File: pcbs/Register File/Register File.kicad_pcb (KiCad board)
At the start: 4 copper layers, 160 parts, among them U201 74HCT574, U202 74HC245, U203 74HC245, U204 74HC245, U301 74HCT574, U302 74HC245, U303 74HC245, U304 74HC245, U401 74HCT574, U402 74HC245, U403 74HC245, U404 74HC245, U501 74HCT574, U502 74HC245, U503 74HC245, U504 74HC245, U601 74HCT574, U602 74HC245, U603 74HC245, U604 74HC245, U701 74HCT574, U702 74HC245, U703 74HC245, U704 74HC245, U801 74HCT574, U802 74HC245, U803 74HC245, U804 74HC245, U901 74HCT574, U902 74HC245, U903 74HC245, U904 74HC245

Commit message: More sketching
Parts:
- added D209: Blue, LED_SMD:LED_0603_1608Metric, F.Cu at (75.2, 52.1)
- added D210: Blue, LED_SMD:LED_0603_1608Metric, F.Cu at (74.9, 69.8)
- added D211: Blue, LED_SMD:LED_0603_1608Metric, F.Cu at (75.2, 87.6)
- added D309: Blue, LED_SMD:LED_0603_1608Metric, F.Cu at (105.7, 79.6)
- added D310: Blue, LED_SMD:LED_0603_1608Metric, F.Cu at (105.7, 82.2)
- added D311: Blue, LED_SMD:LED_0603_1608Metric, F.Cu at (105.7, 84.8)
- added D409: Blue, LED_SMD:LED_0603_1608Metric, F.Cu at (150.0, 149.0)
- added D410: Blue, LED_SMD:LED_0603_1608Metric, F.Cu at (150.0, 151.6)
- added D411: Blue, LED_SMD:LED_0603_1608Metric, F.Cu at (150.0, 154.1)
- added D509: Blue, LED_SMD:LED_0603_1608Metric, F.Cu at (170.1, 158.7)
- added D510: Blue, LED_SMD:LED_0603_1608Metric, F.Cu at (170.1, 161.3)
- added D511: Blue, LED_SMD:LED_0603_1608Metric, F.Cu at (170.1, 163.9)
- added D609: Blue, LED_SMD:LED_0603_1608Metric, F.Cu at (160.0, 168.5)
- added D610: Blue, LED_SMD:LED_0603_1608Metric, F.Cu at (160.0, 171.1)
- added D611: Blue, LED_SMD:LED_0603_1608Metric, F.Cu at (160.0, 173.7)
- added D709: Blue, LED_SMD:LED_0603_1608Metric, F.Cu at (170.1, 149.0)
- added D710: Blue, LED_SMD:LED_0603_1608Metric, F.Cu at (170.1, 151.6)
- added D711: Blue, LED_SMD:LED_0603_1608Metric, F.Cu at (170.1, 154.1)
- added D809: Blue, LED_SMD:LED_0603_1608Metric, F.Cu at (160.0, 158.7)
- added D810: Blue, LED_SMD:LED_0603_1608Metric, F.Cu at (160.0, 161.3)
- added D811: Blue, LED_SMD:LED_0603_1608Metric, F.Cu at (160.0, 163.9)
- added D909: Blue, LED_SMD:LED_0603_1608Metric, F.Cu at (150.0, 158.7)
- added D910: Blue, LED_SMD:LED_0603_1608Metric, F.Cu at (150.0, 161.3)
- added D911: Blue, LED_SMD:LED_0603_1608Metric, F.Cu at (150.0, 163.9)
- added R209: 4k7, Resistor_SMD:R_0603_1608Metric, F.Cu at (71.6, 52.1)
- added R210: 4k7, Resistor_SMD:R_0603_1608Metric, F.Cu at (71.4, 69.8)
- added R211: 4k7, Resistor_SMD:R_0603_1608Metric, F.Cu at (71.4, 87.6)
- added R309: 4k7, Resistor_SMD:R_0603_1608Metric, F.Cu at (109.7, 79.6)
- added R310: 4k7, Resistor_SMD:R_0603_1608Metric, F.Cu at (109.7, 82.1)
- added R311: 4k7, Resistor_SMD:R_0603_1608Metric, F.Cu at (109.7, 84.6)
- added R409: 4k7, Resistor_SMD:R_0603_1608Metric, F.Cu at (154.0, 148.9)
- added R410: 4k7, Resistor_SMD:R_0603_1608Metric, F.Cu at (154.0, 151.4)
- added R411: 4k7, Resistor_SMD:R_0603_1608Metric, F.Cu at (154.0, 153.9)
- added R509: 4k7, Resistor_SMD:R_0603_1608Metric, F.Cu at (174.1, 158.7)
- added R510: 4k7, Resistor_SMD:R_0603_1608Metric, F.Cu at (174.1, 161.2)
- added R511: 4k7, Resistor_SMD:R_0603_1608Metric, F.Cu at (174.1, 163.7)
- added R609: 4k7, Resistor_SMD:R_0603_1608Metric, F.Cu at (164.0, 168.5)
- added R610: 4k7, Resistor_SMD:R_0603_1608Metric, F.Cu at (164.0, 171.0)
- added R611: 4k7, Resistor_SMD:R_0603_1608Metric, F.Cu at (164.0, 173.5)
- added R709: 4k7, Resistor_SMD:R_0603_1608Metric, F.Cu at (174.1, 148.9)
- added R710: 4k7, Resistor_SMD:R_0603_1608Metric, F.Cu at (174.1, 151.4)
- added R711: 4k7, Resistor_SMD:R_0603_1608Metric, F.Cu at (174.1, 153.9)
- added R809: 4k7, Resistor_SMD:R_0603_1608Metric, F.Cu at (164.0, 158.7)
- added R810: 4k7, Resistor_SMD:R_0603_1608Metric, F.Cu at (164.0, 161.2)
- added R811: 4k7, Resistor_SMD:R_0603_1608Metric, F.Cu at (164.0, 163.7)
- added R909: 4k7, Resistor_SMD:R_0603_1608Metric, F.Cu at (154.0, 158.7)
- added R910: 4k7, Resistor_SMD:R_0603_1608Metric, F.Cu at (154.0, 161.2)
- added R911: 4k7, Resistor_SMD:R_0603_1608Metric, F.Cu at (154.0, 163.7)
- moved U302 3.59 mm to (96.5, 61.0)
- moved U203 2.54 mm to (71.1, 78.7)
- moved U204 2.54 mm to (71.1, 96.5)
- moved U202 2.54 mm to (71.1, 61.0)
- moved D301 2.54 mm to (91.4, 27.9)
- moved D302 2.54 mm to (91.4, 30.5)
- moved D303 2.54 mm to (91.4, 33.0)
- moved D304 2.54 mm to (91.4, 35.6)
- moved D305 2.54 mm to (91.4, 38.1)
- moved D306 2.54 mm to (91.4, 40.6)
- moved D307 2.54 mm to (91.4, 43.2)
- moved D308 2.54 mm to (91.4, 45.7)
- moved R301 2.54 mm to (96.5, 27.9)
- moved R302 2.54 mm to (96.5, 30.5)
- moved R303 2.54 mm to (96.5, 33.0)
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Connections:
- U202 pad 19: unconnected-(U202-CE-Pad19) -> /Register 0/~{A_{Enable}}
- U203 pad 19: unconnected-(U203-CE-Pad19) -> /Register 0/~{B_{Enable}}
- U204 pad 19: unconnected-(U204-CE-Pad19) -> /Register 0/~{C_{Enable}}
- U302 pad 19: unconnected-(U302-CE-Pad19) -> /Register 1/~{A_{Enable}}
- U303 pad 19: unconnected-(U303-CE-Pad19) -> /Register 1/~{B_{Enable}}
- U304 pad 19: unconnected-(U304-CE-Pad19) -> /Register 1/~{C_{Enable}}
- U402 pad 19: unconnected-(U402-CE-Pad19) -> /Register 2/~{A_{Enable}}
- U403 pad 19: unconnected-(U403-CE-Pad19) -> /Register 2/~{B_{Enable}}
- U404 pad 19: unconnected-(U404-CE-Pad19) -> /Register 2/~{C_{Enable}}
- U502 pad 19: unconnected-(U502-CE-Pad19) -> /Register 3/~{A_{Enable}}
- U503 pad 19: unconnected-(U503-CE-Pad19) -> /Register 3/~{B_{Enable}}
- U504 pad 19: unconnected-(U504-CE-Pad19) -> /Register 3/~{C_{Enable}}
- U602 pad 19: unconnected-(U602-CE-Pad19) -> /Register 4/~{A_{Enable}}
- U603 pad 19: unconnected-(U603-CE-Pad19) -> /Register 4/~{B_{Enable}}
- U604 pad 19: unconnected-(U604-CE-Pad19) -> /Register 4/~{C_{Enable}}
- U702 pad 19: unconnected-(U702-CE-Pad19) -> /Register 7/~{A_{Enable}}
- U703 pad 19: unconnected-(U703-CE-Pad19) -> /Register 7/~{B_{Enable}}
- U704 pad 19: unconnected-(U704-CE-Pad19) -> /Register 7/~{C_{Enable}}
- U802 pad 19: unconnected-(U802-CE-Pad19) -> /Register 6/~{A_{Enable}}
- U803 pad 19: unconnected-(U803-CE-Pad19) -> /Register 6/~{B_{Enable}}
- U804 pad 19: unconnected-(U804-CE-Pad19) -> /Register 6/~{C_{Enable}}
- U902 pad 19: unconnected-(U902-CE-Pad19) -> /Register 5/~{A_{Enable}}
- U903 pad 19: unconnected-(U903-CE-Pad19) -> /Register 5/~{B_{Enable}}
- U904 pad 19: unconnected-(U904-CE-Pad19) -> /Register 5/~{C_{Enable}}
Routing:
- net /Register 0/r0: track 0.00 -> 83.9 mm, vias 0 -> 1
- net /Register 0/r1: track 0.00 -> 81.1 mm, vias 0 -> 1
- net /Register 0/r2: track 0.00 -> 78.3 mm, vias 0 -> 1
- net /Register 0/r3: track 0.00 -> 73.8 mm, vias 0 -> 1
- net /Register 0/r5: track 0.00 -> 67.6 mm, vias 0 -> 1
- net /Register 0/r6: track 0.00 -> 67.1 mm, vias 0 -> 1
- net /Register 0/r4: track 0.00 -> 67.1 mm, vias 0 -> 1
- net /Register 0/r7: track 0.00 -> 64.6 mm, vias 0 -> 1
- net /Register 1/r0: track 0.00 -> 53.4 mm
- net /Register 1/r4: track 0.00 -> 38.2 mm
- net /Register 1/r3: track 0.00 -> 38.0 mm
- net /Register 1/r5: track 0.00 -> 15.9 mm
- net /Register 1/r6: track 0.00 -> 13.3 mm
- net /Register 1/r1: track 0.00 -> 12.8 mm
- net /Register 1/r7: track 0.00 -> 10.0 mm
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
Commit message: More connecting
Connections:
- D202 pad 2: unconnected-(D202-A-Pad2) -> /Register 0/r1
- D203 pad 2: unconnected-(D203-A-Pad2) -> /Register 0/r2
- D204 pad 2: unconnected-(D204-A-Pad2) -> /Register 0/r3
- D205 pad 2: unconnected-(D205-A-Pad2) -> /Register 0/r4
- D206 pad 2: unconnected-(D206-A-Pad2) -> /Register 0/r5
- D207 pad 2: unconnected-(D207-A-Pad2) -> /Register 0/r6
- D302 pad 2: unconnected-(D302-A-Pad2) -> /Register 1/r1
- D303 pad 2: unconnected-(D303-A-Pad2) -> /Register 1/r2
- D304 pad 2: unconnected-(D304-A-Pad2) -> /Register 1/r3
- D305 pad 2: unconnected-(D305-A-Pad2) -> /Register 1/r4
- D306 pad 2: unconnected-(D306-A-Pad2) -> /Register 1/r5
- D307 pad 2: unconnected-(D307-A-Pad2) -> /Register 1/r6
- D402 pad 2: unconnected-(D402-A-Pad2) -> /Register 2/r1
- D403 pad 2: unconnected-(D403-A-Pad2) -> /Register 2/r2
- D404 pad 2: unconnected-(D404-A-Pad2) -> /Register 2/r3
- D405 pad 2: unconnected-(D405-A-Pad2) -> /Register 2/r4
- D406 pad 2: unconnected-(D406-A-Pad2) -> /Register 2/r5
- D407 pad 2: unconnected-(D407-A-Pad2) -> /Register 2/r6
- D502 pad 2: unconnected-(D502-A-Pad2) -> /Register 3/r1
- D503 pad 2: unconnected-(D503-A-Pad2) -> /Register 3/r2
- D504 pad 2: unconnected-(D504-A-Pad2) -> /Register 3/r3
- D505 pad 2: unconnected-(D505-A-Pad2) -> /Register 3/r4
- D506 pad 2: unconnected-(D506-A-Pad2) -> /Register 3/r5
- D507 pad 2: unconnected-(D507-A-Pad2) -> /Register 3/r6
- D602 pad 2: unconnected-(D602-A-Pad2) -> /Register 4/r1
- D603 pad 2: unconnected-(D603-A-Pad2) -> /Register 4/r2
- D604 pad 2: unconnected-(D604-A-Pad2) -> /Register 4/r3
- D605 pad 2: unconnected-(D605-A-Pad2) -> /Register 4/r4
- D606 pad 2: unconnected-(D606-A-Pad2) -> /Register 4/r5
- D607 pad 2: unconnected-(D607-A-Pad2) -> /Register 4/r6
- D702 pad 2: unconnected-(D702-A-Pad2) -> /Register 7/r1
- D703 pad 2: unconnected-(D703-A-Pad2) -> /Register 7/r2
- D704 pad 2: unconnected-(D704-A-Pad2) -> /Register 7/r3
- D705 pad 2: unconnected-(D705-A-Pad2) -> /Register 7/r4
- D706 pad 2: unconnected-(D706-A-Pad2) -> /Register 7/r5
- D707 pad 2: unconnected-(D707-A-Pad2) -> /Register 7/r6
- D802 pad 2: unconnected-(D802-A-Pad2) -> /Register 6/r1
- D803 pad 2: unconnected-(D803-A-Pad2) -> /Register 6/r2
- D804 pad 2: unconnected-(D804-A-Pad2) -> /Register 6/r3
- D805 pad 2: unconnected-(D805-A-Pad2) -> /Register 6/r4
- D806 pad 2: unconnected-(D806-A-Pad2) -> /Register 6/r5
- D807 pad 2: unconnected-(D807-A-Pad2) -> /Register 6/r6
- D902 pad 2: unconnected-(D902-A-Pad2) -> /Register 5/r1
- D903 pad 2: unconnected-(D903-A-Pad2) -> /Register 5/r2
- D904 pad 2: unconnected-(D904-A-Pad2) -> /Register 5/r3
- D905 pad 2: unconnected-(D905-A-Pad2) -> /Register 5/r4
- D906 pad 2: unconnected-(D906-A-Pad2) -> /Register 5/r5
- D907 pad 2: unconnected-(D907-A-Pad2) -> /Register 5/r6
- U201 pad 1: unconnected-(U201-OE-Pad1) -> GND
- U201 pad 11: unconnected-(U201-Cp-Pad11) -> /Register 0/C_{write}
- U301 pad 1: unconnected-(U301-OE-Pad1) -> GND
- U301 pad 11: unconnected-(U301-Cp-Pad11) -> /Register 1/C_{write}
- U401 pad 1: unconnected-(U401-OE-Pad1) -> GND
- U401 pad 11: unconnected-(U401-Cp-Pad11) -> /Register 2/C_{write}
- U501 pad 1: unconnected-(U501-OE-Pad1) -> GND
- U501 pad 11: unconnected-(U501-Cp-Pad11) -> /Register 3/C_{write}
- U601 pad 1: unconnected-(U601-OE-Pad1) -> GND
- U601 pad 11: unconnected-(U601-Cp-Pad11) -> /Register 4/C_{write}
- U701 pad 1: unconnected-(U701-OE-Pad1) -> GND
- U701 pad 11: unconnected-(U701-Cp-Pad11) -> /Register 7/C_{write}
- U801 pad 1: unconnected-(U801-OE-Pad1) -> GND
- U801 pad 11: unconnected-(U801-Cp-Pad11) -> /Register 6/C_{write}
- U901 pad 1: unconnected-(U901-OE-Pad1) -> GND
- U901 pad 11: unconnected-(U901-Cp-Pad11) -> /Register 5/C_{write}

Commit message: Routing
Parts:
- moved R309 30.5 mm to (96.5, 52.1), turned to 180 degrees
- moved D309 28.0 mm to (100.6, 52.1), turned to 180 degrees
- moved R310 17.9 mm to (96.5, 69.8), turned to 180 degrees
- moved R311 13.5 mm to (96.5, 87.6), turned to 180 degrees
- moved D310 13.3 mm to (100.6, 69.8), turned to 180 degrees
- moved D311 5.82 mm to (100.6, 87.6), turned to 180 degrees
- moved U303 3.59 mm to (96.5, 78.7)
- moved U304 3.59 mm to (96.5, 96.5)
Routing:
- net /Register 1/r1: track 12.8 -> 103.2 mm, vias 0 -> 3
- net /Register 1/r2: track 9.50 -> 98.8 mm, vias 0 -> 3
- net /Register 1/r7: track 10.0 -> 74.2 mm, vias 0 -> 3
- net /Register 1/r6: track 13.3 -> 73.9 mm, vias 0 -> 3
- net /Register 1/r5: track 15.9 -> 73.7 mm, vias 0 -> 3
- net /Register 1/r3: track 38.0 -> 94.5 mm, vias 0 -> 3
- net /Register 1/r0: track 53.4 -> 107.5 mm, vias 0 -> 3
- net /Register 1/r4: track 38.2 -> 73.4 mm, vias 0 -> 3
- net /Register 0/C6: track 26.5 -> 57.1 mm, vias 0 -> 2
- net /Register 0/B5: track 0.00 -> 30.7 mm, vias 0 -> 2
- net /Register 0/C7: track 26.5 -> 57.1 mm, vias 0 -> 2
- net /Register 0/B7: track 0.00 -> 30.7 mm, vias 0 -> 2
- net /Register 0/B6: track 0.00 -> 30.7 mm, vias 0 -> 2
- net /Register 0/C5: track 26.5 -> 57.1 mm, vias 0 -> 2
- net /Register 0/B4: track 0.00 -> 30.7 mm, vias 0 -> 2
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
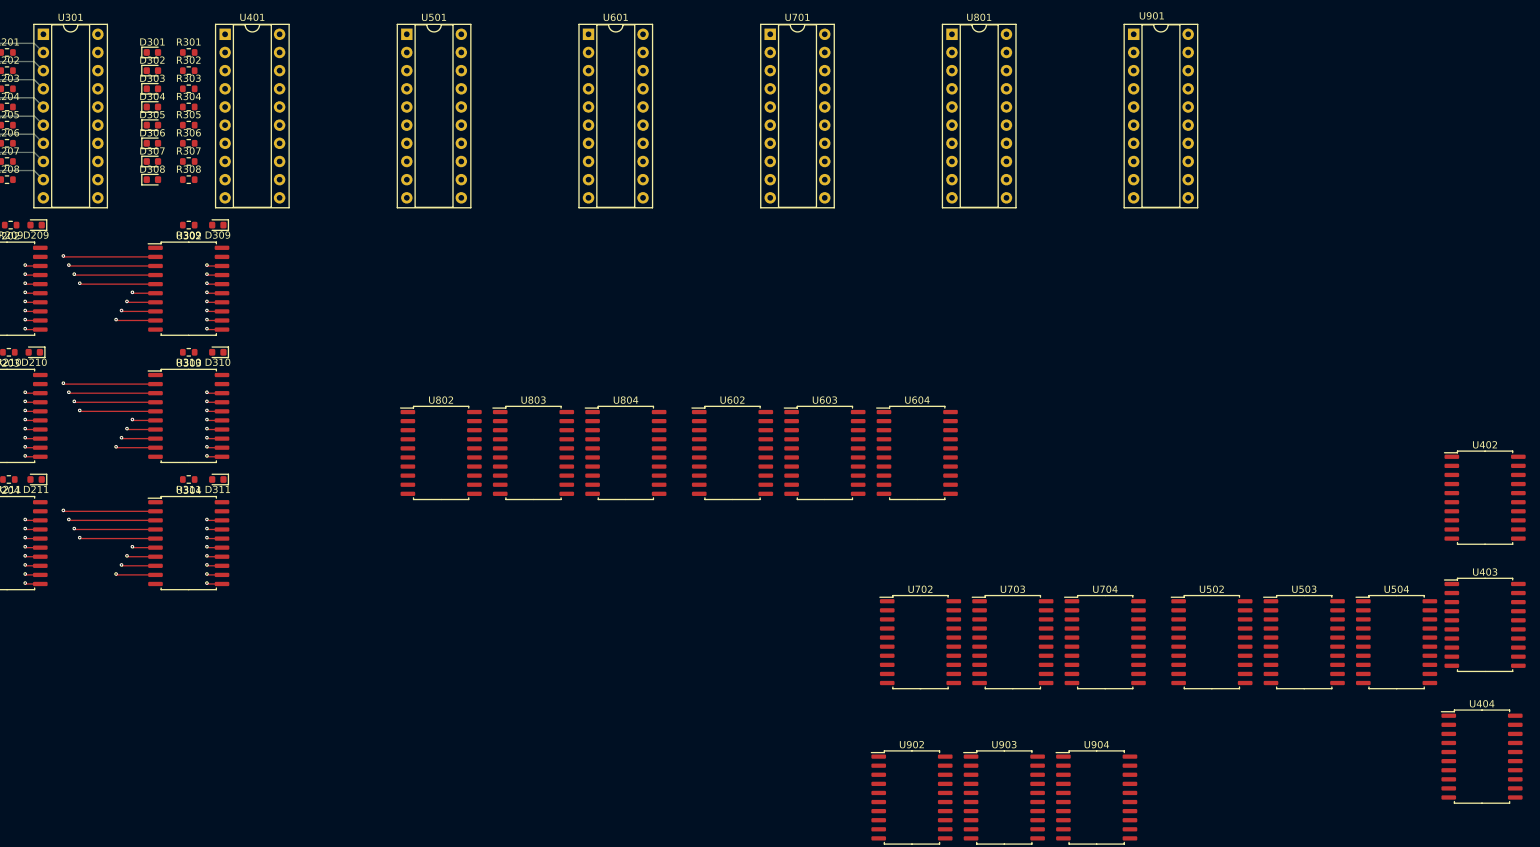
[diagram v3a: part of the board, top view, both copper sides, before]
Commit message: More routing and connecting
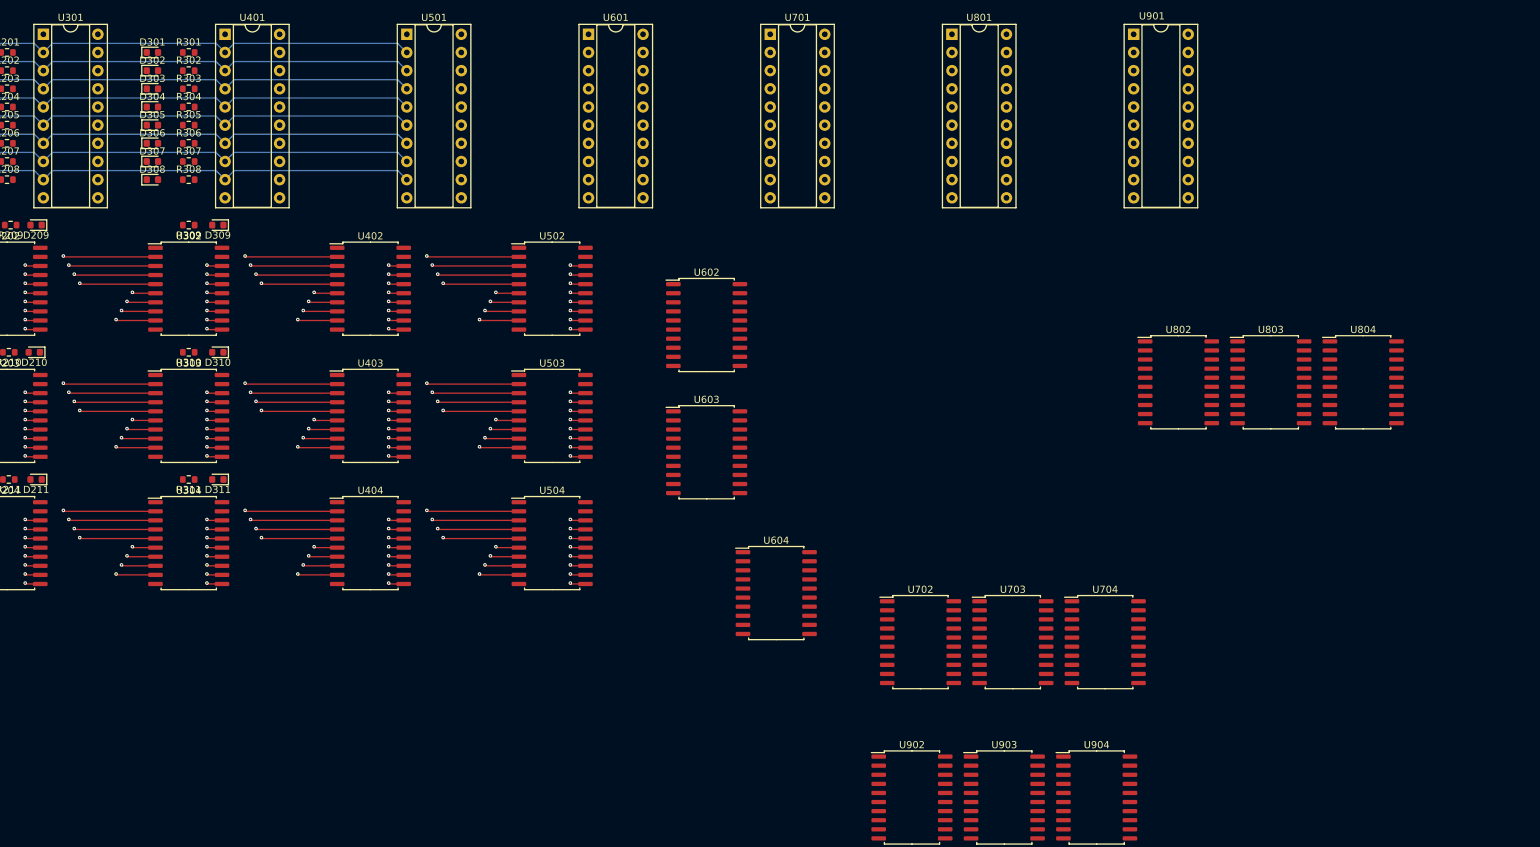
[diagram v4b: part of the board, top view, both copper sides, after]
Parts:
- moved U402 158.5 mm to (121.9, 61.0)
- moved U403 158.5 mm to (121.9, 78.7)
- moved U404 158.2 mm to (121.9, 96.5)
- moved U504 118.8 mm to (147.3, 96.5)
- moved U503 109.8 mm to (147.3, 78.7)
- moved U502 104.6 mm to (147.3, 61.0)
- moved U804 103.5 mm to (260.7, 74.0)
- moved U802 103.5 mm to (234.9, 74.0)
- moved U803 103.5 mm to (247.8, 74.0)
- moved U604 27.8 mm to (178.6, 103.5)
- moved U602 18.2 mm to (168.9, 66.0)
- moved U603 16.5 mm to (168.9, 83.8)
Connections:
- U401 pad 2: /Register 2/C0 -> /Register 0/C0
- U401 pad 3: /Register 2/C1 -> /Register 0/C1
- U401 pad 4: /Register 2/C2 -> /Register 0/C2
- U401 pad 5: /Register 2/C3 -> /Register 0/C3
- U401 pad 6: /Register 2/C4 -> /Register 0/C4
- U401 pad 7: /Register 2/C5 -> /Register 0/C5
- U401 pad 8: /Register 2/C6 -> /Register 0/C6
- U401 pad 9: /Register 2/C7 -> /Register 0/C7
- U402 pad 11: /Register 2/A7 -> /Register 0/A7
- U402 pad 12: /Register 2/A6 -> /Register 0/A6
- U402 pad 13: /Register 2/A5 -> /Register 0/A5
- U402 pad 14: /Register 2/A4 -> /Register 0/A4
- U402 pad 15: /Register 2/A3 -> /Register 0/A3
- U402 pad 16: /Register 2/A2 -> /Register 0/A2
- U402 pad 17: /Register 2/A1 -> /Register 0/A1
- U402 pad 18: /Register 2/A0 -> /Register 0/A0
- U403 pad 11: /Register 2/B7 -> /Register 0/B7
- U403 pad 12: /Register 2/B6 -> /Register 0/B6
- U403 pad 13: /Register 2/B5 -> /Register 0/B5
- U403 pad 14: /Register 2/B4 -> /Register 0/B4
- U403 pad 15: /Register 2/B3 -> /Register 0/B3
- U403 pad 16: /Register 2/B2 -> /Register 0/B2
- U403 pad 17: /Register 2/B1 -> /Register 0/B1
- U403 pad 18: /Register 2/B0 -> /Register 0/B0
- U404 pad 11: /Register 2/C7 -> /Register 0/C7
- U404 pad 12: /Register 2/C6 -> /Register 0/C6
- U404 pad 13: /Register 2/C5 -> /Register 0/C5
- U404 pad 14: /Register 2/C4 -> /Register 0/C4
- U404 pad 15: /Register 2/C3 -> /Register 0/C3
- U404 pad 16: /Register 2/C2 -> /Register 0/C2
- U404 pad 17: /Register 2/C1 -> /Register 0/C1
- U404 pad 18: /Register 2/C0 -> /Register 0/C0
- U501 pad 2: /Register 3/C0 -> /Register 0/C0
- U501 pad 3: /Register 3/C1 -> /Register 0/C1
- U501 pad 4: /Register 3/C2 -> /Register 0/C2
- U501 pad 5: /Register 3/C3 -> /Register 0/C3
- U501 pad 6: /Register 3/C4 -> /Register 0/C4
- U501 pad 7: /Register 3/C5 -> /Register 0/C5
- U501 pad 8: /Register 3/C6 -> /Register 0/C6
- U501 pad 9: /Register 3/C7 -> /Register 0/C7
- U502 pad 11: /Register 3/A7 -> /Register 0/A7
- U502 pad 12: /Register 3/A6 -> /Register 0/A6
- U502 pad 13: /Register 3/A5 -> /Register 0/A5
- U502 pad 14: /Register 3/A4 -> /Register 0/A4
- U502 pad 15: /Register 3/A3 -> /Register 0/A3
- U502 pad 16: /Register 3/A2 -> /Register 0/A2
- U502 pad 17: /Register 3/A1 -> /Register 0/A1
- U502 pad 18: /Register 3/A0 -> /Register 0/A0
- U503 pad 11: /Register 3/B7 -> /Register 0/B7
- U503 pad 12: /Register 3/B6 -> /Register 0/B6
- U503 pad 13: /Register 3/B5 -> /Register 0/B5
- U503 pad 14: /Register 3/B4 -> /Register 0/B4
- U503 pad 15: /Register 3/B3 -> /Register 0/B3
- U503 pad 16: /Register 3/B2 -> /Register 0/B2
- U503 pad 17: /Register 3/B1 -> /Register 0/B1
- U503 pad 18: /Register 3/B0 -> /Register 0/B0
- U504 pad 11: /Register 3/C7 -> /Register 0/C7
- U504 pad 12: /Register 3/C6 -> /Register 0/C6
- U504 pad 13: /Register 3/C5 -> /Register 0/C5
- U504 pad 14: /Register 3/C4 -> /Register 0/C4
- U504 pad 15: /Register 3/C3 -> /Register 0/C3
- U504 pad 16: /Register 3/C2 -> /Register 0/C2
- U504 pad 17: /Register 3/C1 -> /Register 0/C1
- U504 pad 18: /Register 3/C0 -> /Register 0/C0
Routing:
- net /Register 0/C6: track 57.1 -> 167.0 mm, vias 2 -> 4
- net /Register 0/C5: track 57.1 -> 167.0 mm, vias 2 -> 4
- net /Register 0/C7: track 57.1 -> 167.0 mm, vias 2 -> 4
- net /Register 0/C4: track 57.1 -> 167.0 mm, vias 2 -> 4
- net /Register 0/C3: track 56.8 -> 166.1 mm, vias 2 -> 4
- net /Register 0/C2: track 57.1 -> 166.4 mm, vias 2 -> 4
- net /Register 0/C1: track 56.8 -> 166.1 mm, vias 2 -> 4
- net /Register 0/C0: track 56.8 -> 166.1 mm, vias 2 -> 4
- net /Register 2/r0: track 0.00 -> 107.5 mm, vias 0 -> 3
- net /Register 3/r0: track 0.00 -> 107.5 mm, vias 0 -> 3
- net /Register 2/r1: track 0.00 -> 103.2 mm, vias 0 -> 3
- net /Register 3/r1: track 0.00 -> 103.2 mm, vias 0 -> 3
- net /Register 2/r2: track 0.00 -> 98.8 mm, vias 0 -> 3
- net /Register 3/r2: track 0.00 -> 98.8 mm, vias 0 -> 3
- net /Register 2/r3: track 0.00 -> 94.5 mm, vias 0 -> 3
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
